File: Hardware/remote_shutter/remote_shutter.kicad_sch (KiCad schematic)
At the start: 3 parts, among them J1 USB_C_Receptacle_USB2.0

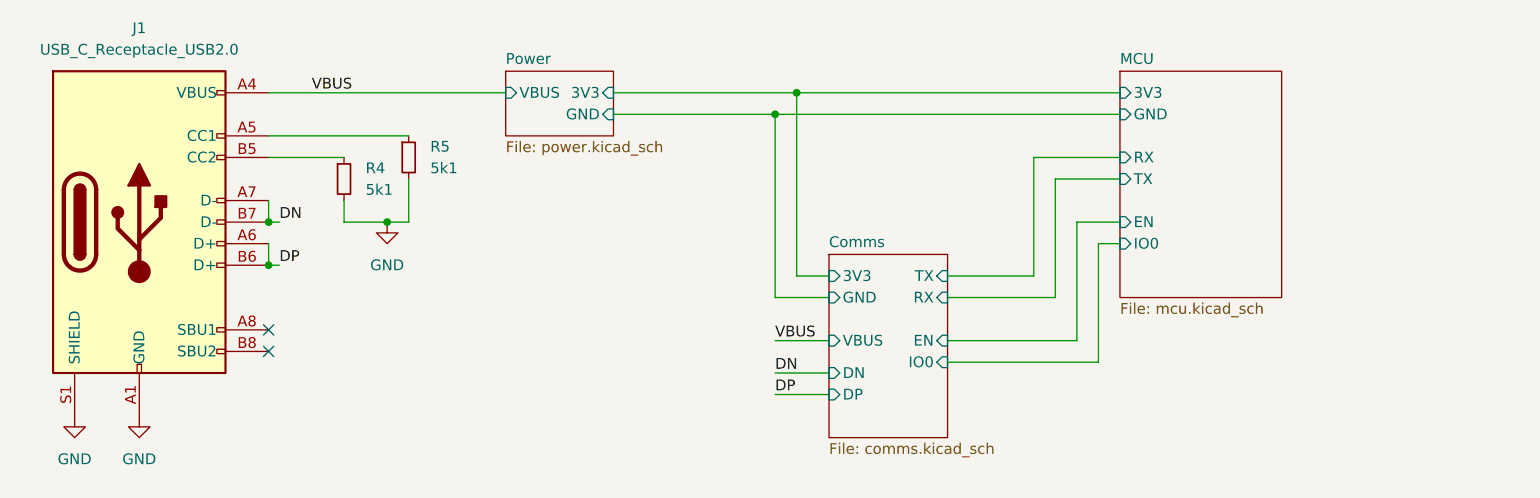
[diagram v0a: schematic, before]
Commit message: Routing USB and charger.
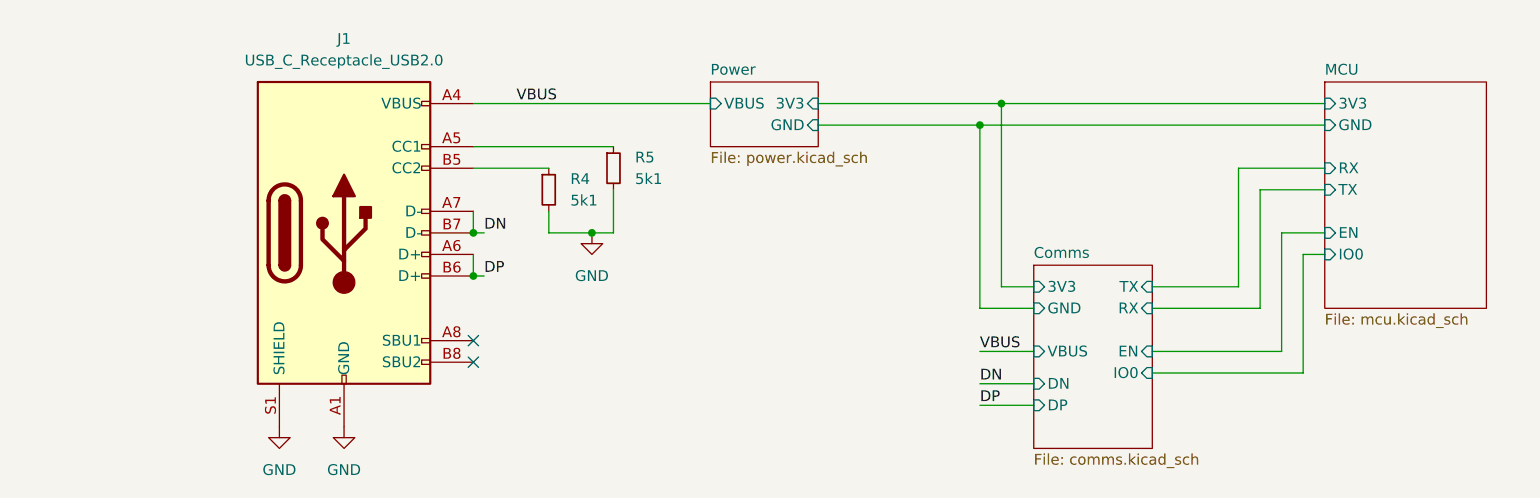
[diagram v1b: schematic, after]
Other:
- moved on the sheet: J1, R4, R5

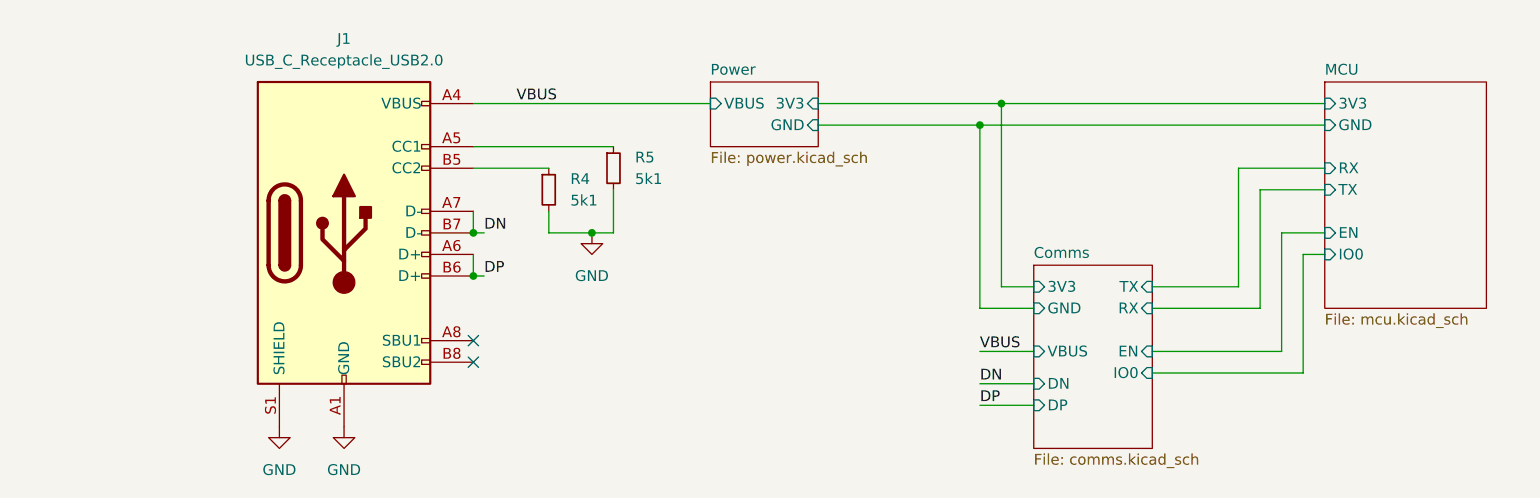
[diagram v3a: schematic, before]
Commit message: Added debug connectors
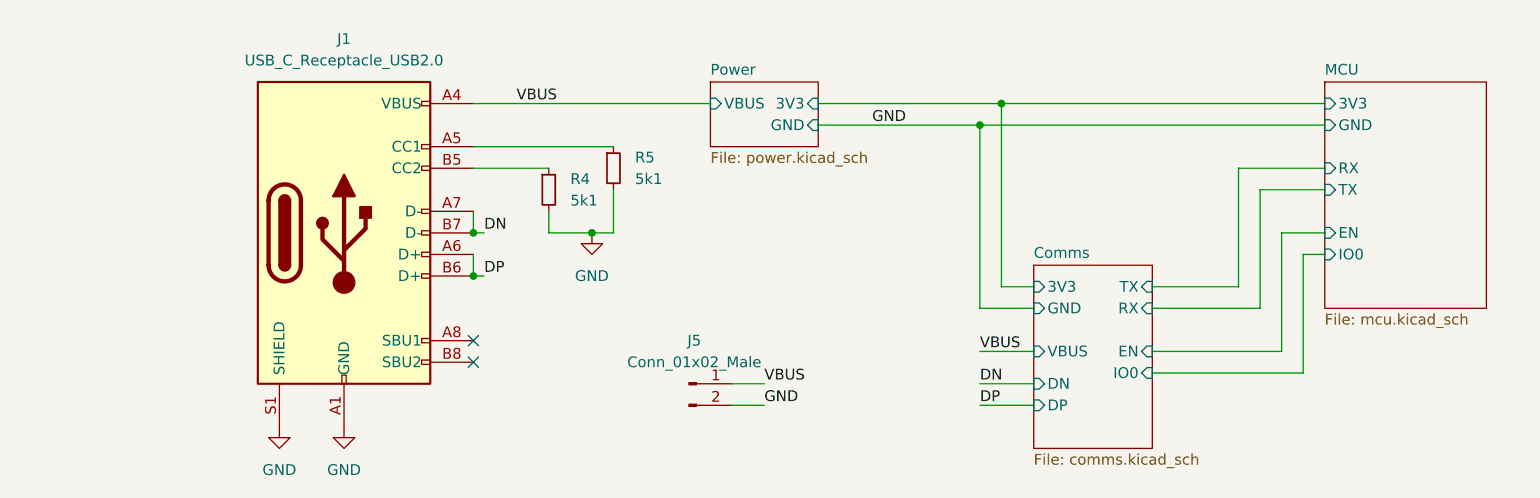
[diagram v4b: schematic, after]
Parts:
- added J5: Conn_01x02_Male, Connector_PinHeader_2.54mm:PinHeader_1x02_P2.54mm_Vertical, symbol Connector:Conn_01x02_Male
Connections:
- net GND: now also J5.2 (Pin_2)
- net VBUS: now also J5.1 (Pin_1)
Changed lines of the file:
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@@
+    (stroke (width 0) (type default) (color 0 0 0 0))
+  )
+  (wire (pts (xy 133.35 105.41) (xy 137.16 105.41))
     (stroke (width 0) (type default) (color 0 0 0 0))
   )
@@
     (stroke (width 0) (type default) (color 0 0 0 0))
   )
+  (wire (pts (xy 133.35 107.95) (xy 137.16 107.95))
+    (stroke (width 0) (type default) (color 0 0 0 0))
+  )
   (wire (pts (xy 193.04 80.01) (xy 203.2 80.01))
     (stroke (width 0) (type default) (color 0 0 0 0))
@@
     (effects (font (size 1.27 1.27)) (justify left bottom))
   )
+  (label "GND" (at 149.86 74.93 0)
+    (effects (font (size 1.27 1.27)) (justify left bottom))
+  )
   (label "VBUS" (at 107.95 72.39 0)
     (effects (font (size 1.27 1.27)) (justify left bottom))
@@
     (effects (font (size 1.27 1.27)) (justify left bottom))
   )
+  (label "GND" (at 137.16 107.95 0)
+    (effects (font (size 1.27 1.27)) (justify left bottom))
+  )
   (label "VBUS" (at 162.56 101.6 0)
     (effects (font (size 1.27 1.27)) (justify left bottom))
   )
   (label "DN" (at 104.14 87.63 0)
+    (effects (font (size 1.27 1.27)) (justify left bottom))
+  )
+  (label "VBUS" (at 137.16 105.41 0)
     (effects (font (size 1.27 1.27)) (justify left bottom))
   )
@@
     (pin "2")
   )
+  (symbol (lib_id "Connector:Conn_01x02_Male") (at 128.27 105.41 0) (unit 1)
+    (in_bom yes) (on_board yes) (fields_autoplaced)
+    (property "Reference" "J5" (id 0) (at 128.905 100.33 0))
+    (property "Value" "Conn_01x02_Male" (id 1) (at 128.905 102.87 0))
+    (property "Footprint" "Connector_PinHeader_2.54mm:PinHeader_1x02_P2.54mm_Vertical" (id 2) (at 128.27 105.41 0)
+      (effects (font (size 1.27 1.27)) hide)
+    )
+    (property "Datasheet" "~" (id 3) (at 128.27 105.41 0)
+      (effects (font (size 1.27 1.27)) hide)
+    )
+    (pin "1")
+    (pin "2")
+  )
   (sheet (at 130.81 69.85) (size 12.7 7.62) (fields_autoplaced)
     (stroke (width 0.1524) (type solid) (color 0 0 0 0))
@@
       (reference "J4") (unit 1) (value "Buzzer") (footprint "Connector_PinSocket_2.54mm:PinSocket_1x02_P2.54mm_Vertical")
     )
+    (path "/fd15a230-5096-44ed-a3bf-9e339f35aae3"
+      (reference "J5") (unit 1) (value "Conn_01x02_Male") (footprint "Connector_PinHeader_2.54mm:PinHeader_1x02_P2.54mm_Vertical")
+    )
     (path "/0c902a43-b121-4fe4-bfa1-34ed8f238e77/c0402d3c-8995-4a8f-a6a2-124a39df8636"
       (reference "J6") (unit 1) (value "Switch") (footprint "Connector_PinHeader_2.54mm:PinHeader_1x03_P2.54mm_Vertical")
     )
+    (path "/76614985-77bf-4b33-94c5-94a8e5c748f5/3bdbae3e-46de-4ed6-9c83-f3b64c64291d"
+      (reference "J7") (unit 1) (value "Conn_01x06_Male") (footprint "Connector_PinHeader_2.54mm:PinHeader_1x06_P2.54mm_Vertical")
+    )
     (path "/76614985-77bf-4b33-94c5-94a8e5c748f5/44fe3afb-1c9a-46d5-8310-2d9db6eb3664/7e48265c-802c-44ca-ba29-6fca3dd0ca2d"

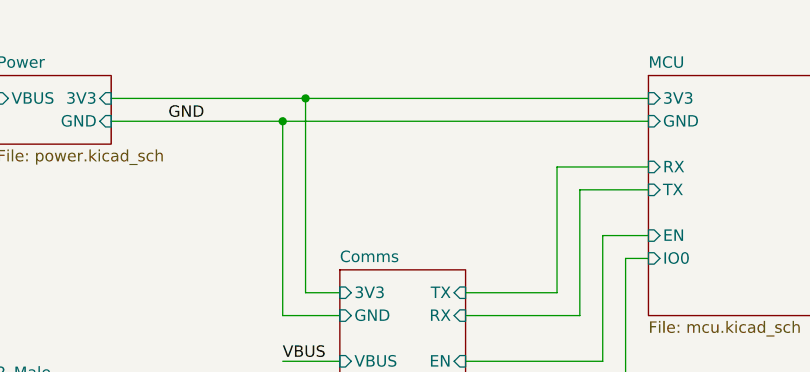
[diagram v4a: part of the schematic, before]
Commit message: Changed layout for better routing. New routing.
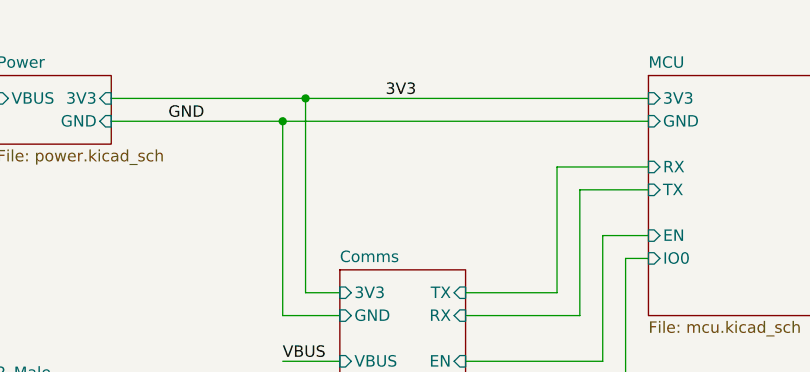
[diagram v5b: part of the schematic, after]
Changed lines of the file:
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@@
+    (effects (font (size 1.27 1.27)) (justify left bottom))
+  )
+  (label "3V3" (at 173.99 72.39 0)
     (effects (font (size 1.27 1.27)) (justify left bottom))
   )
